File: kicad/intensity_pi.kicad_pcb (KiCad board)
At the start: 4 copper layers, 62.8 x 172 mm, 126 parts, among them J1 Input A, J2 Input B / Setpoint, J3 Monitor, J4 Output, J7 select 1, J8 Screw_Terminal_01x03, Q1 2N7002E, Q2 2N7002E, SW1 SW_SPDT, SW2 SW_SPDT, SW3 SW_SPDT, SW5 EG6100-ND, U1 LM4040DBZ-5, U10 OPA189, U11 PC817, U12 OPA189, U13 BUF634A, U14 TMUX6123, U17 TMUX6123, U18 OPA189, U19 L7815, U2 LM4040DBZ-5, U20 OPA189, U21 OPA189, U22 4x Comparator, U23 L7915, U3 INA849, U4 INA849, U5 OPA189, U7 OPA189, U8 BUF634A, U9 LM317_TO-252

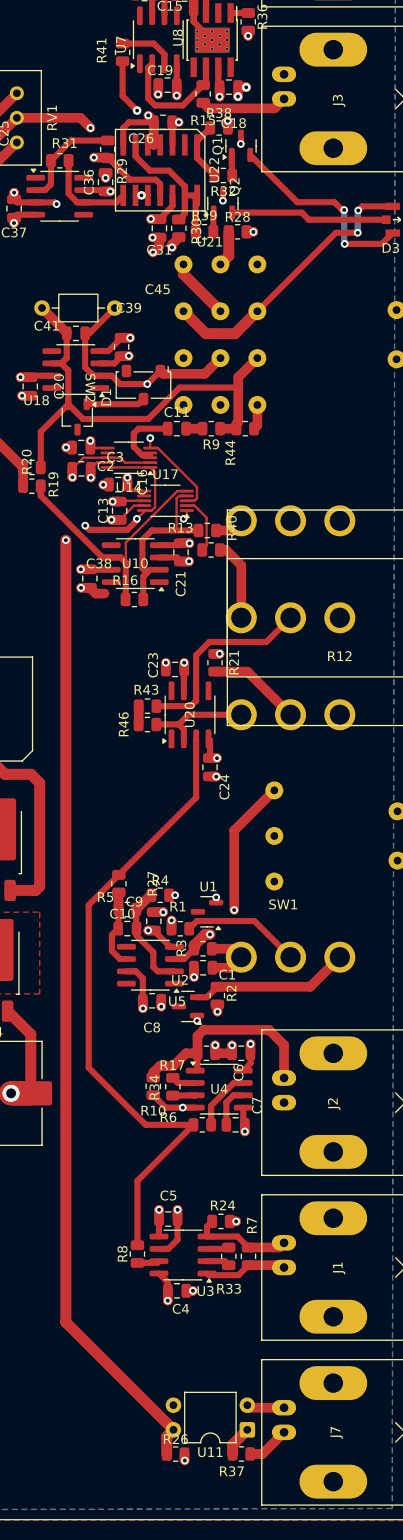
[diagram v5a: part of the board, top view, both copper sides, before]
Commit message: Updated PI control Layout, fixed circular pot footprint so that CW rotation decreases R
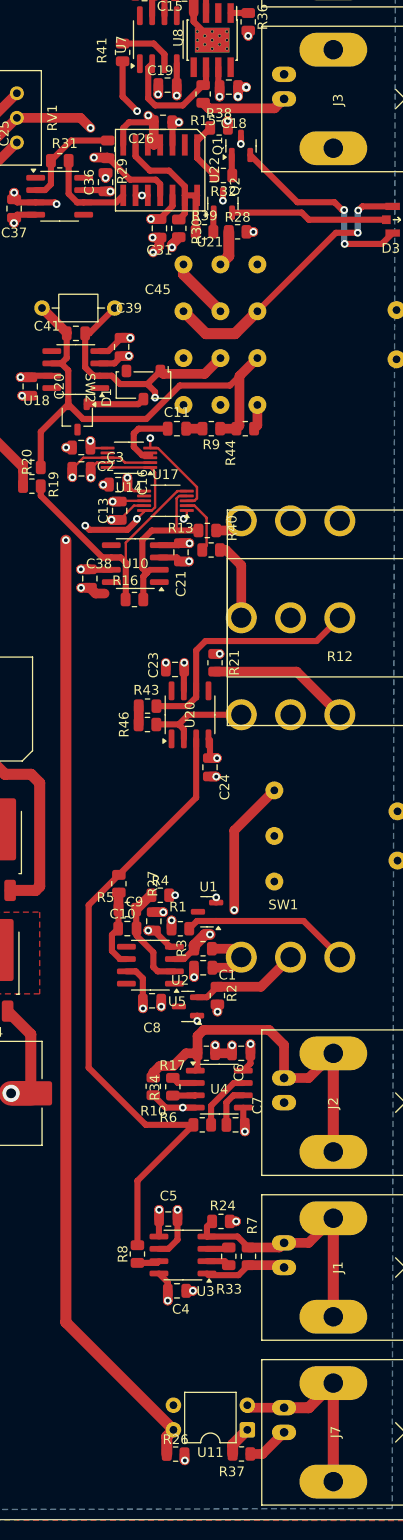
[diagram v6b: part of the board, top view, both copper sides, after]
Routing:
- net Net-(J2-Ext): track 22.8 -> 39.1 mm
- net Net-(J1-Ext): track 10.4 -> 26.7 mm
- net Net-(J7-Ext): track 3.89 -> 20.2 mm
- net Error_signal: track 91.2 -> 98.0 mm
- net Net-(R14-Pad1): track 9.63 -> 14.7 mm
- net Net-(U2-A): track 16.4 -> 11.4 mm
- net Net-(U1-K): track 12.3 -> 17.4 mm
- net Net-(D1-A): track 49.5 -> 50.1 mm

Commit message: Revert change to Library Footprint for switch, update schematic to use resistance between pins 2,3 as starting at maximum, decreasing down on CW rotation
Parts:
- renumbered R14 to RV4, R12 to RV5
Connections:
- R21 pad 2: Net-(R14-Pad1) -> Net-(R21-Pad2)
- RV3 pad 1: Error_signal -> GND
- RV3 pad 3: GND -> Error_signal
- RV4 pad 1: Net-(R14-Pad1) -> unconnected-(RV4-Pad1)
- RV4 pad 3: (no net) -> Net-(R21-Pad2)
- RV5 pad 1: Error_signal -> unconnected-(RV5-Pad1)
- RV5 pad 3: (no net) -> Error_signal
- RV8 pad 1: Net-(U1-K) -> Net-(U2-A)
- RV8 pad 3: Net-(U2-A) -> Net-(U1-K)
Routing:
- net Net-(R21-Pad2): track 0.00 -> 14.7 mm
- net Net-(R14-Pad1): track 14.7 -> 0.00 mm

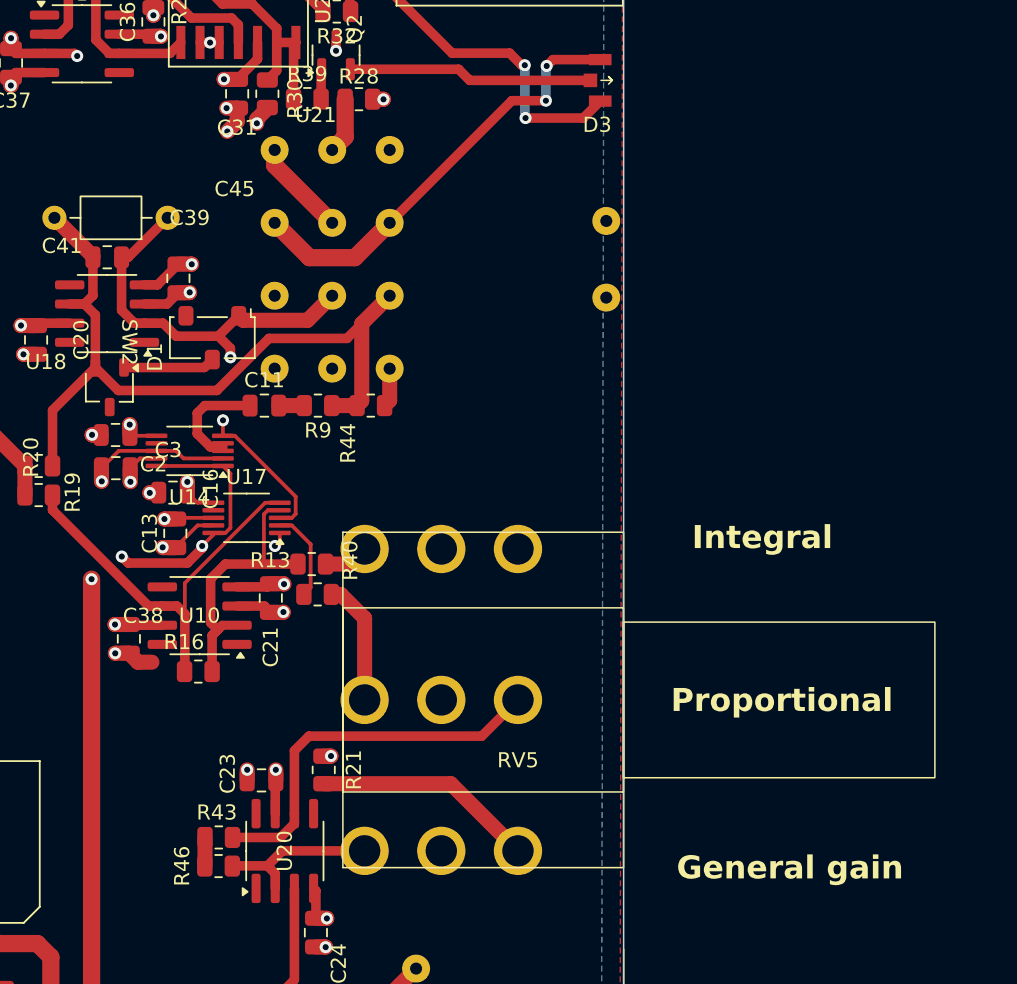
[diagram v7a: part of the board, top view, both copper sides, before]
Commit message: Connected other leg of Pots, added 3d models from manufacturer for switch+pots
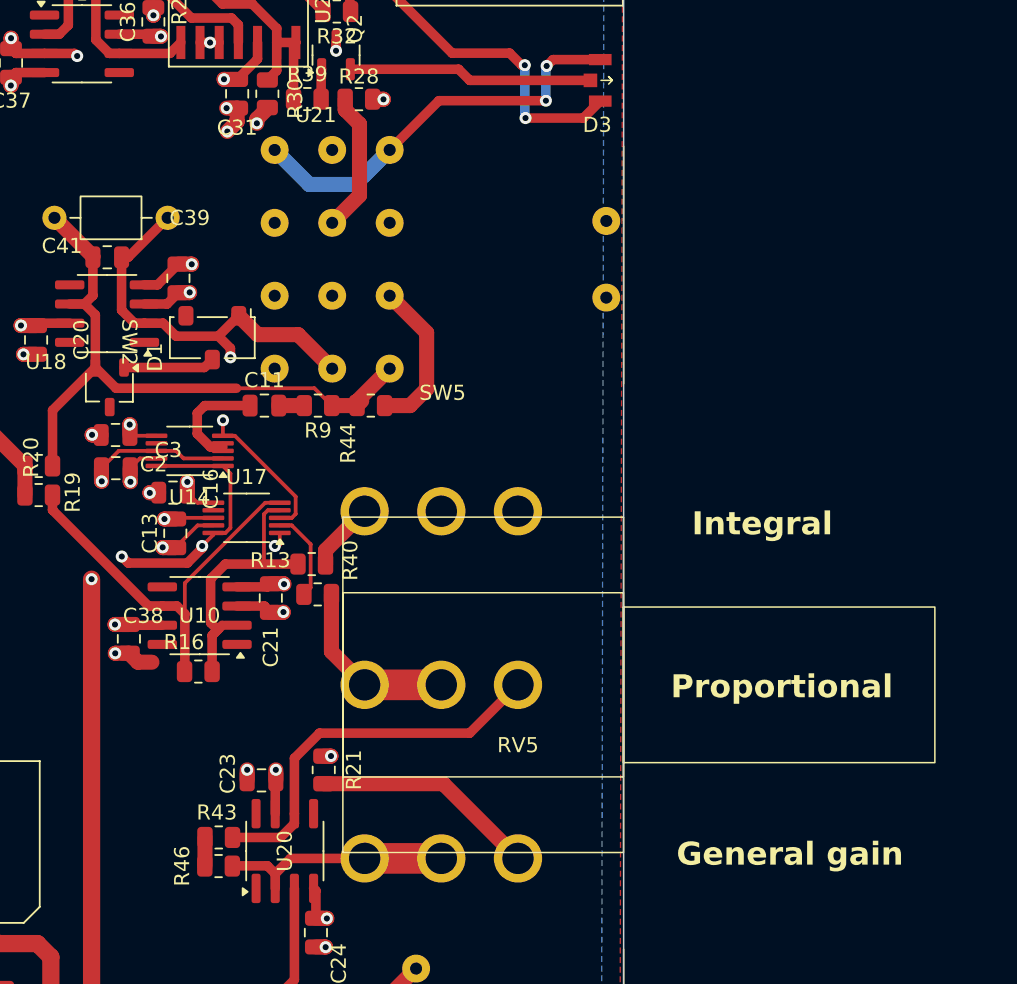
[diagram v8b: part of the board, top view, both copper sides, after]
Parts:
- SW5: moved to F.Cu
- moved RV3 2.50 mm to (5.75, -26.5)
- moved RV5 1.00 mm to (5.75, -15.0)
- moved RV4 0.50 mm to (5.75, -3.50)
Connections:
- RV4 pad 1: unconnected-(RV4-Pad1) -> Net-(U20--)
- RV5 pad 1: unconnected-(RV5-Pad1) -> Net-(R40-Pad1)
- SW5 pad 1: unconnected-(SW5-Pad1) -> Net-(D1-A)
- SW5 pad 10: Net-(R44-Pad1) -> Net-(D3-A)
- SW5 pad 12: unconnected-(SW5-Pad12) -> Net-(D3-A)
- SW5 pad 2: Net-(R28-Pad2) -> Net-(SW2-A)
- SW5 pad 4: Net-(D3-A) -> Net-(R44-Pad1)
- SW5 pad 6: Net-(D3-A) -> unconnected-(SW5-Pad6)
- SW5 pad 7: Net-(D1-A) -> unconnected-(SW5-Pad7)
- SW5 pad 8: Net-(SW2-A) -> Net-(R28-Pad2)
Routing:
- net Net-(R44-Pad1): track 2.59 -> 10.4 mm
- net Net-(D1-A): track 50.1 -> 42.3 mm
- net Net-(R28-Pad2): track 3.72 -> 9.34 mm
- net Net-(U20--): track 10.9 -> 15.4 mm
- net Net-(R40-Pad1): track 8.26 -> 12.0 mm
- net Net-(D3-A): track 29.3 -> 27.3 mm
- net Net-(R13-Pad1): track 3.00 -> 4.57 mm
- net Error_signal: track 98.0 -> 97.1 mm
- net Net-(SW2-A): track 39.6 -> 40.3 mm
